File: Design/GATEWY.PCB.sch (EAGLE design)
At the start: 29 parts, among them IC1 FT232RL, SW1 SWITCH-TACTILE, SW2 RA_BUTTON, U1 WS2801, X1 USBPTH

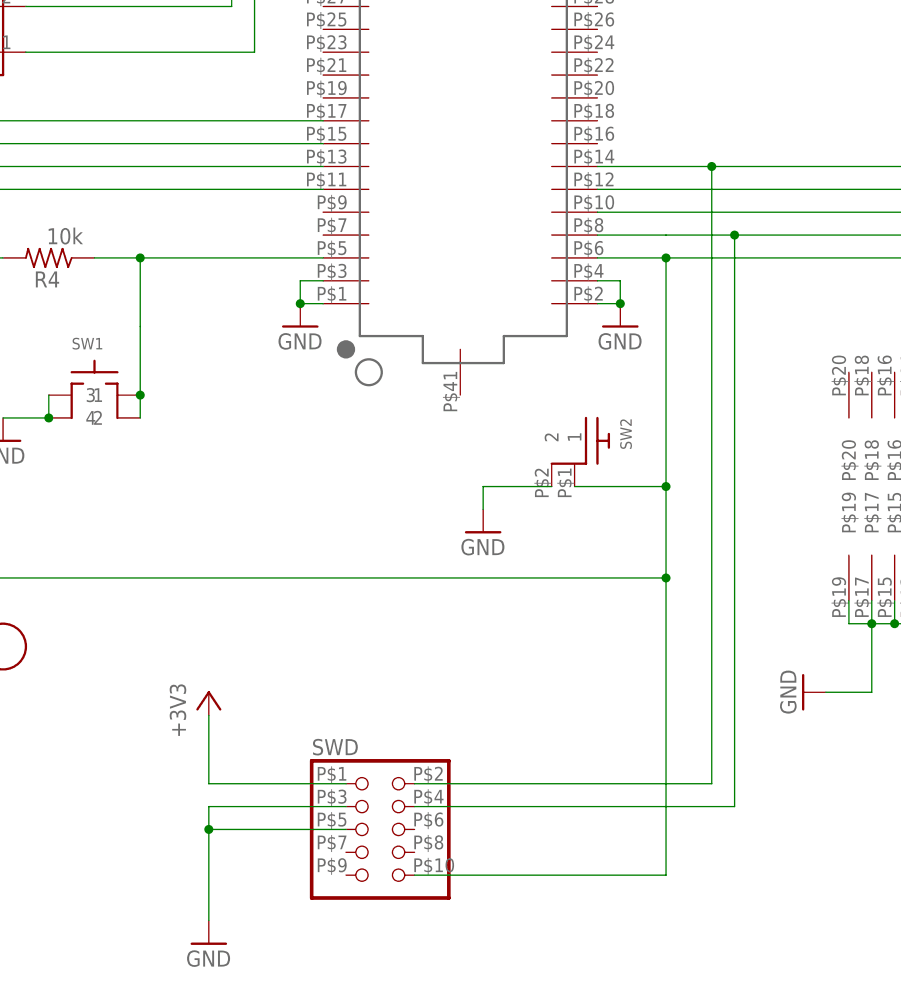
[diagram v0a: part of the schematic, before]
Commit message: Change the JTAG header to SMT
Also remove the SWD header.
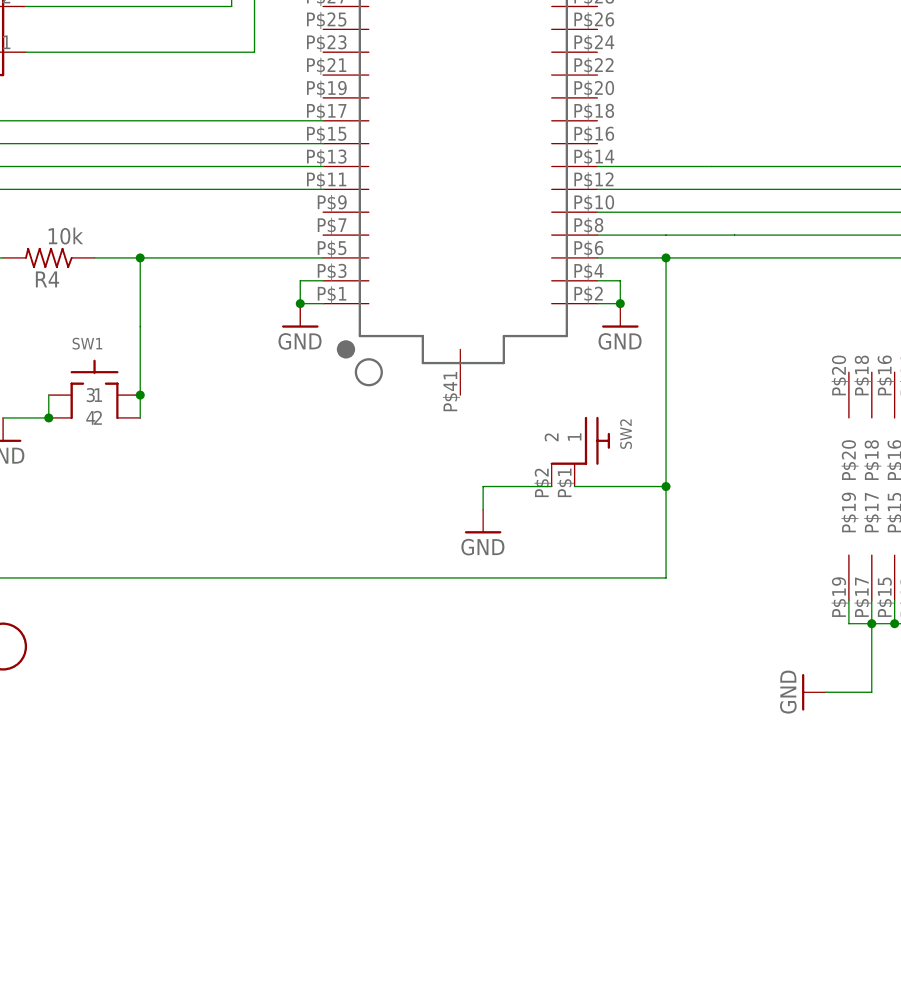
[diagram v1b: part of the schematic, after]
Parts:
- removed SWD: (no value), KW2:PINHD-2X5SMALL
- JTAG: value 2X10JTAG -> 2X10JTAGSMD; device KW2:2X10JTAG -> KW2:2X10JTAGSMD
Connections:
- net +3V3: no longer SWD.1
- net GND: no longer SWD.3, SWD.5
- net N$18: no longer SWD.4
- net N$6: no longer SWD.2
- net SW2: no longer SWD.10
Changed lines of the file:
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@@
 <attribute name="MFGP" value="CRCW080524R0FKEA"/>
 </part>
-<part name="JTAG" library="KW2" deviceset="2X10JTAG" device="" value="2X10JTAG"/>
+<part name="JTAG" library="KW2" deviceset="2X10JTAG" device="SMD" value="2X10JTAGSMD"/>
 <part name="+3V7" library="supply1" deviceset="+3V3" device=""/>
 <part name="GND8" library="supply1" deviceset="GND" device=""/>
@@
 <attribute name="MFGP" value="MICROSMD050F-2"/>
 </part>
-<part name="SWD" library="KW2" deviceset="PINHD-2X5" device="SMALL"/>
-<part name="+3V5" library="supply1" deviceset="+3V3" device=""/>
-<part name="GND4" library="supply1" deviceset="GND" device=""/>
 </parts>
 <sheets>
@@
 <attribute name="MFGP" x="-203.2" y="-40.64" size="1.778" layer="96" rot="R90" display="off"/>
 </instance>
-<instance part="SWD" gate="A" x="0" y="-99.06"/>
-<instance part="+3V5" gate="G$1" x="-17.78" y="-83.82"/>
-<instance part="GND4" gate="1" x="-17.78" y="-111.76"/>
 </instances>
 <busses>
@@
 <pinref part="X1" gate="G$1" pin="GND"/>
 </segment>
-<segment>
-<pinref part="SWD" gate="A" pin="5"/>
-<pinref part="GND4" gate="1" pin="GND"/>
-<wire x1="-2.54" y1="-99.06" x2="-17.78" y2="-99.06" width="0.1524" layer="91"/>
-<wire x1="-17.78" y1="-99.06" x2="-17.78" y2="-109.22" width="0.1524" layer="91"/>
-<pinref part="SWD" gate="A" pin="3"/>
-<wire x1="-2.54" y1="-96.52" x2="-17.78" y2="-96.52" width="0.1524" layer="91"/>
-<wire x1="-17.78" y1="-96.52" x2="-17.78" y2="-99.06" width="0.1524" layer="91"/>
-<junction x="-17.78" y="-99.06"/>
-</segment>
 </net>
 <net name="+3V3" class="1">
@@
 <pinref part="+3V4" gate="G$1" pin="+3V3"/>
 </segment>
-<segment>
-<pinref part="SWD" gate="A" pin="1"/>
-<pinref part="+3V5" gate="G$1" pin="+3V3"/>
-<wire x1="-2.54" y1="-93.98" x2="-17.78" y2="-93.98" width="0.1524" layer="91"/>
-<wire x1="-17.78" y1="-93.98" x2="-17.78" y2="-86.36" width="0.1524" layer="91"/>
-</segment>
 </net>
 <net name="N$4" class="0">
@@
 <wire x1="40.64" y1="-33.02" x2="73.66" y2="-33.02" width="0.1524" layer="91"/>
 <wire x1="73.66" y1="-33.02" x2="73.66" y2="-48.26" width="0.1524" layer="91"/>
-<pinref part="SWD" gate="A" pin="4"/>
-<wire x1="5.08" y1="-96.52" x2="40.64" y2="-96.52" width="0.1524" layer="91"/>
-<wire x1="40.64" y1="-96.52" x2="40.64" y2="-33.02" width="0.1524" layer="91"/>
-<junction x="40.64" y="-33.02"/>
 </segment>
 </net>
@@
 <wire x1="38.1" y1="-25.4" x2="76.2" y2="-25.4" width="0.1524" layer="91"/>
 <wire x1="76.2" y1="-25.4" x2="76.2" y2="-48.26" width="0.1524" layer="91"/>
-<pinref part="SWD" gate="A" pin="2"/>
-<wire x1="5.08" y1="-93.98" x2="38.1" y2="-93.98" width="0.1524" layer="91"/>
-<wire x1="38.1" y1="-93.98" x2="38.1" y2="-25.4" width="0.1524" layer="91"/>
-<junction x="38.1" y="-25.4"/>
 </segment>
 </net>
@@
 <pinref part="SW2" gate="G$1" pin="1"/>
 <wire x1="22.86" y1="-60.96" x2="33.02" y2="-60.96" width="0.1524" layer="91"/>
-<pinref part="SWD" gate="A" pin="10"/>
-<wire x1="5.08" y1="-104.14" x2="33.02" y2="-104.14" width="0.1524" layer="91"/>
-<wire x1="33.02" y1="-104.14" x2="33.02" y2="-71.12" width="0.1524" layer="91"/>
 <junction x="33.02" y="-60.96"/>
 <pinref part="IC1" gate="1" pin="CBUS0"/>
@@
 <wire x1="-66.04" y1="-68.58" x2="-66.04" y2="-71.12" width="0.1524" layer="91"/>
 <wire x1="-66.04" y1="-71.12" x2="33.02" y2="-71.12" width="0.1524" layer="91"/>
-<junction x="33.02" y="-71.12"/>
-</segment>
-</net>
+</segment>
+</net>

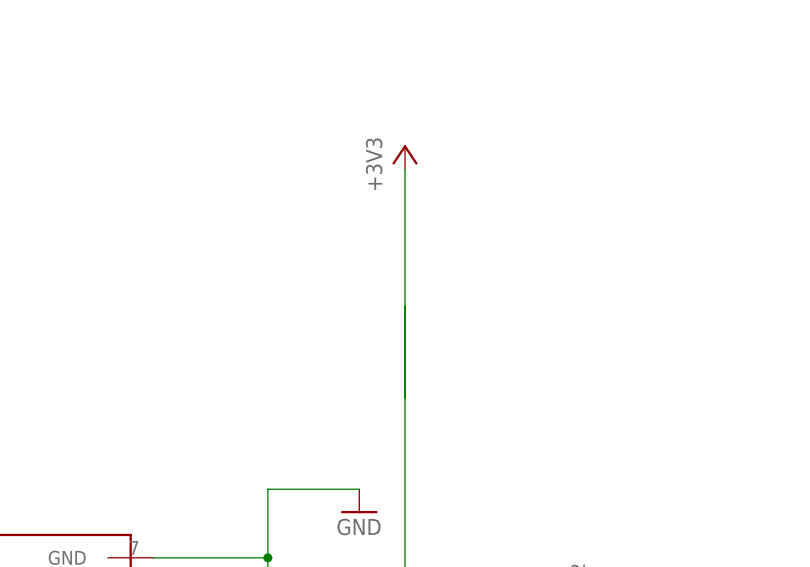
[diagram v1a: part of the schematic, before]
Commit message: Fix a problem with 3.3V
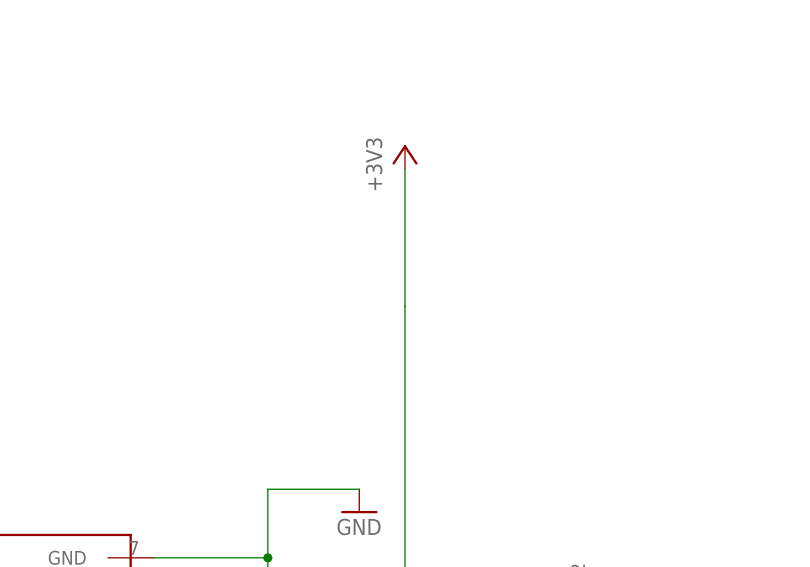
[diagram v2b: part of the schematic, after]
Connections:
- net N$18 renamed JTAG_CLK
- net N$20 renamed JTAG_TDI
- net N$6 renamed JTAG_TMS
- net N$8 renamed JTAG_TDO
- net SW2 renamed RESET
- removed net N$1: KW2.+3V3@1, KW2.+3V3@2
- net +3V3: now also KW2.+3V3@1, KW2.+3V3@2

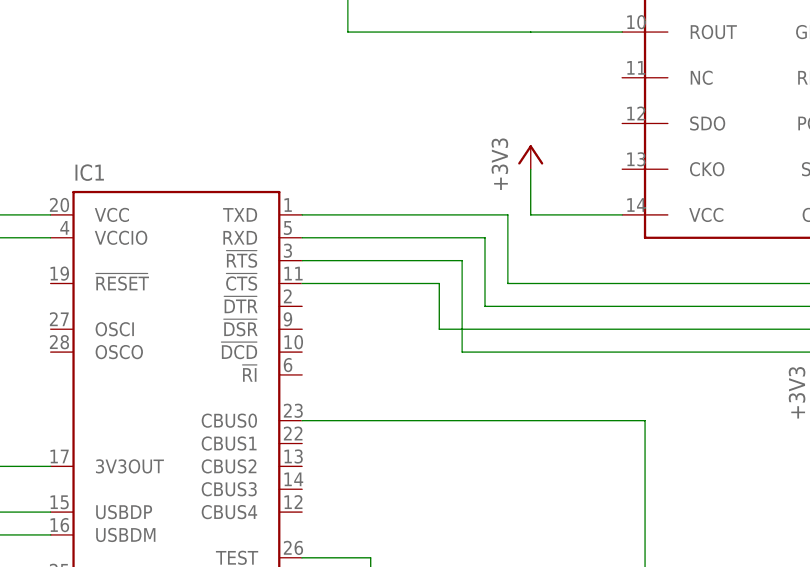
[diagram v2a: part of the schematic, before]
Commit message: Fix the FTDI UART pins.
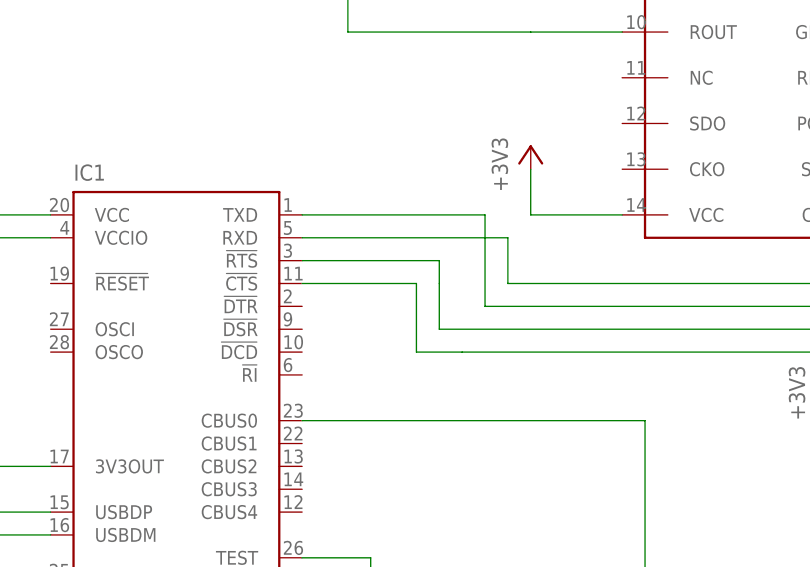
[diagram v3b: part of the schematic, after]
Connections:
- removed net N$15: IC1.TXD, KW2.PTD7/MADC0_SE22/CMT_IRO/UART0_TX/FTM0_CH7/FTM0_FLT1
- removed net N$2: IC1.!RTS, KW2.PTD4/LLWU_P14/MADC0_SE21/SPI0_PCS1/!UART0_RTS!/FTM0_CH4/EWM_IN/GPIO_BSM_FRAME
- removed net N$3: IC1.!CTS, KW2.PTD5/ADC0_SE6B/SPI0_PCS2/!UART0_CTS!/!UART0_COL!/FTM0_CH5/!EWM_OUT
- removed net N$9: IC1.RXD, KW2.PTD6/LLWU_P15/ADC0_SE7B/SPI0_PCS3/UART0_RX/FTM0_CH6/FTM0_FLT0
- new net CTS: IC1.!RTS, KW2.PTD5/ADC0_SE6B/SPI0_PCS2/!UART0_CTS!/!UART0_COL!/FTM0_CH5/!EWM_OUT
- new net RTS: IC1.!CTS, KW2.PTD4/LLWU_P14/MADC0_SE21/SPI0_PCS1/!UART0_RTS!/FTM0_CH4/EWM_IN/GPIO_BSM_FRAME
- new net RX: IC1.TXD, KW2.PTD6/LLWU_P15/ADC0_SE7B/SPI0_PCS3/UART0_RX/FTM0_CH6/FTM0_FLT0
- new net TX: IC1.RXD, KW2.PTD7/MADC0_SE22/CMT_IRO/UART0_TX/FTM0_CH7/FTM0_FLT1
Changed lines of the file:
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@@
 </segment>
 </net>
-<net name="N$2" class="0">
+<net name="RTS" class="0">
 <segment>
 <pinref part="KW2" gate="G$1" pin="PTD4/LLWU_P14/MADC0_SE21/SPI0_PCS1/!UART0_RTS!/FTM0_CH4/EWM_IN/GPIO_BSM_FRAME"/>
 <wire x1="-5.08" y1="-27.94" x2="-86.36" y2="-27.94" width="0.1524" layer="91"/>
-<wire x1="-86.36" y1="-27.94" x2="-86.36" y2="-17.78" width="0.1524" layer="91"/>
-<pinref part="IC1" gate="1" pin="!RTS"/>
-<wire x1="-86.36" y1="-17.78" x2="-104.14" y2="-17.78" width="0.1524" layer="91"/>
+<wire x1="-86.36" y1="-27.94" x2="-91.44" y2="-27.94" width="0.1524" layer="91"/>
+<pinref part="IC1" gate="1" pin="!CTS"/>
+<wire x1="-91.44" y1="-27.94" x2="-91.44" y2="-20.32" width="0.1524" layer="91"/>
+<wire x1="-91.44" y1="-20.32" x2="-104.14" y2="-20.32" width="0.1524" layer="91"/>
 </segment>
 </net>
-<net name="N$3" class="0">
+<net name="CTS" class="0">
 <segment>
 <pinref part="KW2" gate="G$1" pin="PTD5/ADC0_SE6B/SPI0_PCS2/!UART0_CTS!/!UART0_COL!/FTM0_CH5/!EWM_OUT"/>
 <wire x1="-5.08" y1="-25.4" x2="-88.9" y2="-25.4" width="0.1524" layer="91"/>
 <wire x1="-88.9" y1="-25.4" x2="-88.9" y2="-20.32" width="0.1524" layer="91"/>
-<pinref part="IC1" gate="1" pin="!CTS"/>
-<wire x1="-88.9" y1="-20.32" x2="-104.14" y2="-20.32" width="0.1524" layer="91"/>
+<pinref part="IC1" gate="1" pin="!RTS"/>
+<wire x1="-88.9" y1="-20.32" x2="-88.9" y2="-17.78" width="0.1524" layer="91"/>
+<wire x1="-88.9" y1="-17.78" x2="-104.14" y2="-17.78" width="0.1524" layer="91"/>
 </segment>
 </net>
-<net name="N$9" class="0">
+<net name="RX" class="0">
 <segment>
 <pinref part="KW2" gate="G$1" pin="PTD6/LLWU_P15/ADC0_SE7B/SPI0_PCS3/UART0_RX/FTM0_CH6/FTM0_FLT0"/>
 <wire x1="-5.08" y1="-22.86" x2="-83.82" y2="-22.86" width="0.1524" layer="91"/>
 <wire x1="-83.82" y1="-22.86" x2="-83.82" y2="-15.24" width="0.1524" layer="91"/>
-<pinref part="IC1" gate="1" pin="RXD"/>
-<wire x1="-83.82" y1="-15.24" x2="-104.14" y2="-15.24" width="0.1524" layer="91"/>
+<pinref part="IC1" gate="1" pin="TXD"/>
+<wire x1="-83.82" y1="-15.24" x2="-83.82" y2="-12.7" width="0.1524" layer="91"/>
+<wire x1="-83.82" y1="-12.7" x2="-104.14" y2="-12.7" width="0.1524" layer="91"/>
 </segment>
 </net>
-<net name="N$15" class="0">
+<net name="TX" class="0">
 <segment>
 <pinref part="KW2" gate="G$1" pin="PTD7/MADC0_SE22/CMT_IRO/UART0_TX/FTM0_CH7/FTM0_FLT1"/>
 <wire x1="-5.08" y1="-20.32" x2="-81.28" y2="-20.32" width="0.1524" layer="91"/>
-<wire x1="-81.28" y1="-20.32" x2="-81.28" y2="-12.7" width="0.1524" layer="91"/>
-<pinref part="IC1" gate="1" pin="TXD"/>
-<wire x1="-81.28" y1="-12.7" x2="-104.14" y2="-12.7" width="0.1524" layer="91"/>
+<wire x1="-81.28" y1="-20.32" x2="-81.28" y2="-15.24" width="0.1524" layer="91"/>
+<pinref part="IC1" gate="1" pin="RXD"/>
+<wire x1="-81.28" y1="-15.24" x2="-104.14" y2="-15.24" width="0.1524" layer="91"/>
 </segment>
 </net>

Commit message: Fix the design so it generates a correct BOM
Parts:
- JTAG: MFGN (none) -> Sullins; MFGP (none) -> GRPB102VWQS-RC
- LED1: MFGN (none) -> Cree; MFGP (none) -> CLV1A-FKB-CK1N1G1BB7R4S3
- SW2: MFGN (none) -> TE Connectivity; MFGP (none) -> 2-1825027-0
- U1: MFGN (none) -> WorldSemi; MFGP (none) -> WS2801
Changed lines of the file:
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@@
 <part name="+3V1" library="supply1" deviceset="+3V3" device=""/>
 <part name="GND6" library="supply1" deviceset="GND" device=""/>
-<part name="U1" library="GW-devices" deviceset="WS2801" device="" value="WS2801"/>
+<part name="U1" library="GW-devices" deviceset="WS2801" device="" value="WS2801">
+<attribute name="MFGN" value="WorldSemi"/>
+<attribute name="MFGP" value="WS2801"/>
+</part>
 <part name="GND7" library="supply1" deviceset="GND" device=""/>
 <part name="R1" library="GW-devices" deviceset="RF-R" device="0805" value="24Ohm">
@@
 <attribute name="MFGP" value="CRCW080524R0FKEA"/>
 </part>
-<part name="JTAG" library="KW2" deviceset="2X10JTAG" device="SMD" value="2X10JTAGSMD"/>
+<part name="JTAG" library="KW2" deviceset="2X10JTAG" device="SMD" value="2X10JTAGSMD">
+<attribute name="MFGN" value="Sullins"/>
+<attribute name="MFGP" value="GRPB102VWQS-RC"/>
+</part>
 <part name="+3V7" library="supply1" deviceset="+3V3" device=""/>
 <part name="GND8" library="supply1" deviceset="GND" device=""/>
-<part name="SW2" library="KW2" deviceset="RA_BUTTON" device="" value="RA_BUTTON"/>
+<part name="SW2" library="KW2" deviceset="RA_BUTTON" device="" value="RA_BUTTON">
+<attribute name="MFGN" value="TE Connectivity"/>
+<attribute name="MFGP" value="2-1825027-0"/>
+</part>
 <part name="GND11" library="supply1" deviceset="GND" device=""/>
 <part name="R4" library="GW-devices" deviceset="RF-R" device="0805" value="10k">
@@
 </part>
 <part name="+3V9" library="supply1" deviceset="+3V3" device=""/>
-<part name="LED1" library="KW2" deviceset="RGLBED" device="" value="RGLBED"/>
+<part name="LED1" library="KW2" deviceset="RGLBED" device="" value="RGLBED">
+<attribute name="MFGN" value="Cree"/>
+<attribute name="MFGP" value="CLV1A-FKB-CK1N1G1BB7R4S3"/>
+</part>
 <part name="U$14" library="adafruit" deviceset="FIDUCIAL" device="" value="">
 <attribute name="NOTES" value="DNP"/>
@@
 <instance part="+3V1" gate="G$1" x="-10.16" y="63.5"/>
 <instance part="GND6" gate="1" x="-40.64" y="-55.88"/>
-<instance part="U1" gate="G$1" x="-55.88" y="2.54" rot="R180"/>
+<instance part="U1" gate="G$1" x="-55.88" y="2.54" rot="R180">
+<attribute name="MFGN" x="-55.88" y="2.54" size="1.778" layer="96" rot="R180" display="off"/>
+<attribute name="MFGP" x="-55.88" y="2.54" size="1.778" layer="96" rot="R180" display="off"/>
+</instance>
 <instance part="GND7" gate="1" x="-15.24" y="22.86"/>
 <instance part="R1" gate="&gt;NAME" x="-33.02" y="12.7">
@@
 <attribute name="MFGP" x="-33.02" y="2.54" size="1.778" layer="96" display="off"/>
 </instance>
-<instance part="JTAG" gate="G$1" x="66.04" y="-60.96" rot="MR270"/>
+<instance part="JTAG" gate="G$1" x="66.04" y="-60.96" rot="MR270">
+<attribute name="MFGN" x="66.04" y="-60.96" size="1.778" layer="96" rot="MR270" display="off"/>
+<attribute name="MFGP" x="66.04" y="-60.96" size="1.778" layer="96" rot="MR270" display="off"/>
+</instance>
 <instance part="+3V7" gate="G$1" x="81.28" y="-83.82" rot="R270"/>
 <instance part="GND8" gate="1" x="48.26" y="-83.82" rot="R270"/>
-<instance part="SW2" gate="G$1" x="22.86" y="-60.96"/>
+<instance part="SW2" gate="G$1" x="22.86" y="-60.96">
+<attribute name="MFGN" x="22.86" y="-60.96" size="1.778" layer="96" display="off"/>
+<attribute name="MFGP" x="22.86" y="-60.96" size="1.778" layer="96" display="off"/>
+</instance>
 <instance part="GND11" gate="1" x="12.7" y="-66.04"/>
 <instance part="R4" gate="&gt;NAME" x="-35.56" y="-35.56" smashed="yes" rot="R180">
@@
 </instance>
 <instance part="+3V9" gate="G$1" x="-45.72" y="-30.48"/>
-<instance part="LED1" gate="G$1" x="-91.44" y="40.64" rot="R90"/>
+<instance part="LED1" gate="G$1" x="-91.44" y="40.64" rot="R90">
+<attribute name="MFGN" x="-91.44" y="40.64" size="1.778" layer="96" rot="R90" display="off"/>
+<attribute name="MFGP" x="-91.44" y="40.64" size="1.778" layer="96" rot="R90" display="off"/>
+</instance>
 <instance part="U$14" gate="G$1" x="-91.44" y="-78.74">
 <attribute name="NOTES" x="-91.44" y="-78.74" size="1.778" layer="96" display="off"/>
